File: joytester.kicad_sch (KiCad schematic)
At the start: 43 parts, among them J1 DB9_Male, J2 USB_B, J3 USB_C_Receptacle_PowerOnly_6P, J4 USB_B_Mini, J5 USB_B_Micro, SW1 C64MODESW, SW2 POWER, SW3 POWER, U1 4070, U2 74HC86

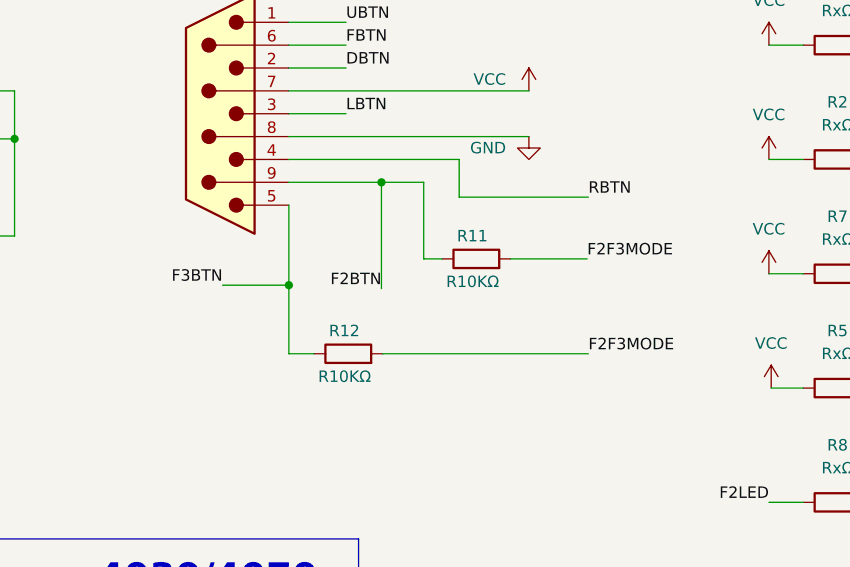
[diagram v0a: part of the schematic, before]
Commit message: update of Micro USB footprint
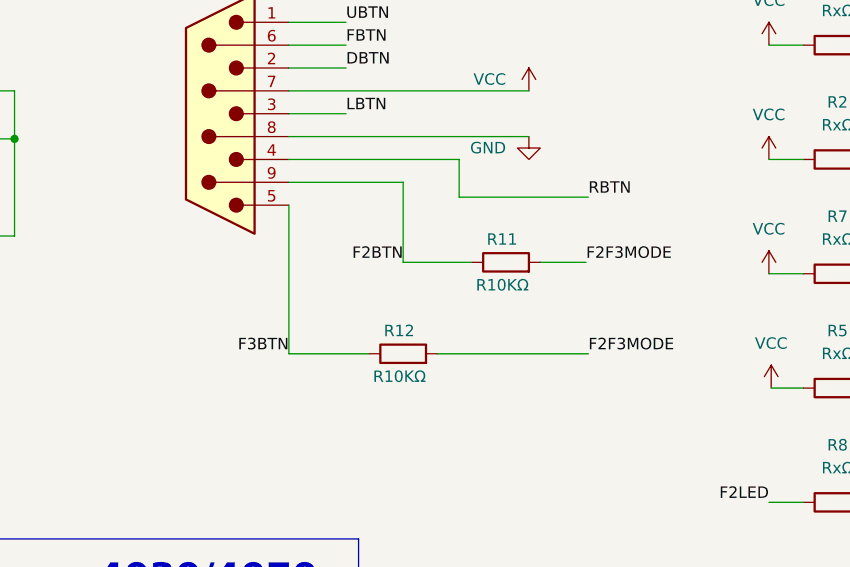
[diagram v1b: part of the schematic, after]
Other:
- moved on the sheet: R11, R12
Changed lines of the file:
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@@
 	)
 	(junction
-		(at 213.487 50.8)
-		(diameter 0)
-		(color 0 0 0 0)
-	)
-	(junction
 		(at 29.972 25.4)
 		(diameter 0)
@@
 	)
 	(junction
-		(at 203.2 62.23)
-		(diameter 0)
-		(color 0 0 0 0)
-	)
-	(junction
 		(at 35.56 69.723)
 		(diameter 0)
@@
 	(wire
 		(pts
-			(xy 213.614 69.85) (xy 236.474 69.85)
+			(xy 219.71 69.85) (xy 236.474 69.85)
 		)
 		(stroke
@@
 	(wire
 		(pts
-			(xy 227.838 59.309) (xy 236.347 59.309)
-		)
-		(stroke
-			(width 0)
-			(type default)
-		)
-	)
-	(wire
-		(pts
 			(xy 256.794 73.66) (xy 260.35 73.66)
 		)
@@
 	(wire
 		(pts
-			(xy 203.2 69.85) (xy 205.994 69.85)
+			(xy 203.2 69.85) (xy 212.09 69.85)
 		)
 		(stroke
@@
 	(wire
 		(pts
-			(xy 203.2 69.85) (xy 203.2 62.23)
+			(xy 203.2 53.34) (xy 203.2 69.85)
 		)
 		(stroke
@@
 	(wire
 		(pts
-			(xy 218.186 50.8) (xy 218.186 59.309)
-		)
-		(stroke
-			(width 0)
-			(type default)
-		)
-	)
-	(wire
-		(pts
 			(xy 209.55 43.18) (xy 203.2 43.18)
 		)
@@
 	(wire
 		(pts
-			(xy 195.834 62.23) (xy 203.2 62.23)
-		)
-		(stroke
-			(width 0)
-			(type default)
-		)
-	)
-	(wire
-		(pts
 			(xy 100.076 80.899) (xy 96.012 80.899)
 		)
@@
 	(wire
 		(pts
-			(xy 281.94 116.84) (xy 275.59 116.84)
+			(xy 231.14 59.69) (xy 236.22 59.69)
 		)
 		(stroke
@@
 	(wire
 		(pts
-			(xy 213.487 50.8) (xy 218.186 50.8)
+			(xy 281.94 116.84) (xy 275.59 116.84)
 		)
 		(stroke
@@
 	(wire
 		(pts
-			(xy 203.2 53.34) (xy 203.2 62.23)
-		)
-		(stroke
-			(width 0)
-			(type default)
-		)
-	)
-	(wire
-		(pts
 			(xy 52.451 148.209) (xy 52.451 144.653)
 		)
@@
 	(wire
 		(pts
-			(xy 203.2 50.8) (xy 213.487 50.8)
+			(xy 203.2 50.8) (xy 215.9 50.8)
 		)
 		(stroke
@@
 	(wire
 		(pts
-			(xy 218.186 59.309) (xy 220.218 59.309)
+			(xy 215.9 50.8) (xy 215.9 59.69)
 		)
 		(stroke
@@
 	(wire
 		(pts
-			(xy 29.972 25.4) (xy 29.972 33.274)
+			(xy 215.9 59.69) (xy 223.52 59.69)
 		)
 		(stroke
@@
 	(wire
 		(pts
-			(xy 234.95 140.843) (xy 234.95 142.24)
+			(xy 29.972 25.4) (xy 29.972 33.274)
 		)
 		(stroke
@@
 	(wire
 		(pts
-			(xy 209.55 38.1) (xy 203.2 38.1)
+			(xy 234.95 140.843) (xy 234.95 142.24)
 		)
 		(stroke
@@
 	(wire
 		(pts
-			(xy 84.709 44.323) (xy 84.709 41.529)
+			(xy 209.55 38.1) (xy 203.2 38.1)
 		)
 		(stroke
@@
 	(wire
 		(pts
-			(xy 213.487 62.611) (xy 213.487 50.8)
+			(xy 84.709 44.323) (xy 84.709 41.529)
 		)
 		(stroke
@@
 	)
 	(label "F3BTN"
-		(at 195.834 62.23 180)
+		(at 203.2 69.85 180)
 		(effects
 			(font
@@
 	)
 	(label "F2BTN"
-		(at 213.487 62.611 180)
+		(at 215.9 59.69 180)
 		(effects
 			(font
@@
 	)
 	(label "F2F3MODE"
-		(at 236.347 59.309 0)
+		(at 236.22 59.69 0)
 		(effects
 			(font
@@
 	(symbol
 		(lib_id "Device:R")
-		(at 224.028 59.309 90)
+		(at 227.33 59.69 90)
 		(unit 1)
 		(exclude_from_sim no)
@@
 		(dnp no)
 		(property "Reference" "R11"
-			(at 225.298 56.769 90)
+			(at 228.6 57.15 90)
 			(effects
 				(font
@@
 		)
 		(property "Value" "R10KΩ"
-			(at 226.568 61.849 90)
+			(at 229.87 62.23 90)
 			(effects
 				(font
@@
 		)
 		(property "Footprint" "misc:R_Axial_DIN0207_L6.3mm_D2.5mm_P10.16mm_Horizontal_Oval"
-			(at 224.028 61.087 90)
+			(at 227.33 61.468 90)
 			(effects
 				(font
@@
 		)
 		(property "Datasheet" "~"
-			(at 224.028 59.309 0)
+			(at 227.33 59.69 0)
 			(effects
 				(font
@@
 		)
 		(property "Description" ""
-			(at 224.028 59.309 0)
+			(at 227.33 59.69 0)
 			(effects
 				(font
@@
 	(symbol
 		(lib_id "Device:R")
-		(at 209.804 69.85 90)
+		(at 215.9 69.85 90)
 		(unit 1)
 		(exclude_from_sim no)
@@
 		(dnp no)
 		(property "Reference" "R12"
-			(at 211.074 67.31 90)
+			(at 217.17 67.31 90)
 			(effects
 				(font
@@
 		)
 		(property "Value" "R10KΩ"
-			(at 212.344 72.39 90)
+			(at 218.44 72.39 90)
 			(effects
 				(font
@@
 		)
 		(property "Footprint" "misc:R_Axial_DIN0207_L6.3mm_D2.5mm_P10.16mm_Horizontal_Oval"
-			(at 209.804 71.628 90)
+			(at 215.9 71.628 90)
 			(effects
 				(font
@@
 		)
 		(property "Datasheet" "~"
-			(at 209.804 69.85 0)
+			(at 215.9 69.85 0)
 			(effects
 				(font
@@
 		)
 		(property "Description" ""
-			(at 209.804 69.85 0)
+			(at 215.9 69.85 0)
 			(effects
 				(font
